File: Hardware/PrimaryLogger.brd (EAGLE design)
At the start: 52.1 x 77.1 mm, 72 parts, among them J1 CONN_42.54_SCREW, J2 CONN_42.54_SCREW, J3 CONN_42.54_SCREW, J4 CONN_42.54_SCREW, J5 CONN_32.54_SCREW, Q1 DMG3404, Q2 DMG3404, U1 MIC2005, U2 MIC2005, U25 SN74AUP3G34DCU, U3 TPL5010DDC, U4 TXS0102DCU, U5 SN74LVC1G3157SC70, U6 TCS3400, U7 SHTC3DFN, U8 MCP23008QFN, U9 MCP7940SOIC

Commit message: Documentation and folder structure updates
Moved around the folder structure, added board pictures, and added to README
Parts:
- JP1, JP2, JP3, JP4, JP5, JP6, JP8: device bschulz:SMT-JUMPER_3_1-NC_PASTE_SILK -> SparkFun-Jumpers:SMT-JUMPER_3_1-NC_PASTE_SILK
- JP10: device bschulz:SMT-JUMPER_2_NO_SILK -> SparkFun-Jumpers:SMT-JUMPER_2_NO_SILK
- JP7, JP9: device bschulz:SMT-JUMPER_2_NC_PASTE_SILK -> SparkFun-Jumpers:SMT-JUMPER_2_NC_PASTE_SILK
- R8: value 10k -> 100k

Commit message: Further documentation updates
Moved production files around, updated BoM in hardware and part libraries links to support that (DNP values issue)
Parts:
- JP1, JP2, JP3, JP4, JP5, JP6, JP8: device SparkFun-Jumpers:SMT-JUMPER_3_1-NC_PASTE_SILK -> bschulz:SMT-JUMPER_3_1-NC_PASTE_SILK
- JP10: device SparkFun-Jumpers:SMT-JUMPER_2_NO_SILK -> bschulz:SMT-JUMPER_2_NO_SILK
- JP9: device SparkFun-Jumpers:SMT-JUMPER_2_NC_PASTE_SILK -> bschulz:SMT-JUMPER_2_NC_PASTE_SILK
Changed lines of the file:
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@@
 <layer number="115" name="ReferenceISLANDS" color="7" fill="1" visible="no" active="yes"/>
 <layer number="116" name="Patch_BOT" color="7" fill="1" visible="no" active="yes"/>
+<layer number="117" name="PM_Ref" color="7" fill="1" visible="no" active="no"/>
 <layer number="118" name="Rect_Pads" color="7" fill="1" visible="no" active="yes"/>
+<layer number="119" name="PF_Ref" color="7" fill="1" visible="no" active="no"/>
+<layer number="120" name="WFL_Ref" color="7" fill="1" visible="no" active="no"/>
 <layer number="121" name="_tsilk" color="7" fill="1" visible="no" active="yes"/>
 <layer number="122" name="_bsilk" color="7" fill="1" visible="no" active="yes"/>
@@
 <attribute name="NAME" x="11.557" y="22.098" size="0.6096" layer="25" font="vector" ratio="15" rot="R90" align="center"/>
 </element>
-<element name="JP1" library="SparkFun-Jumpers" library_urn="urn:adsk.eagle:library:528" package="SMT-JUMPER_3_1-NC_PASTE_SILK" package3d_urn="urn:adsk.eagle:package:39293/1" value="JUMPER-SMT_3_1-NC_PASTE_SILK" x="30.48" y="51.181" smashed="yes" rot="MR90">
+<element name="JP1" library="bschulz" package="SMT-JUMPER_3_1-NC_PASTE_SILK" package3d_urn="urn:adsk.eagle:package:39293/1" value="JUMPER-SMT_3_1-NC_PASTE_SILK" x="30.48" y="51.181" smashed="yes" rot="MR90">
+<attribute name="DIGIKEY" value="DNP" x="30.48" y="51.181" size="1.778" layer="28" rot="MR90" display="off"/>
+<attribute name="MF" value="N/A" x="30.48" y="51.181" size="1.778" layer="28" rot="MR90" display="off"/>
+<attribute name="MPN" value="N/A" x="30.48" y="51.181" size="1.778" layer="28" rot="MR90" display="off"/>
 <attribute name="NAME" x="31.623" y="51.181" size="0.6096" layer="26" font="vector" ratio="20" rot="MR90" align="bottom-center"/>
 </element>
-<element name="JP2" library="SparkFun-Jumpers" library_urn="urn:adsk.eagle:library:528" package="SMT-JUMPER_3_1-NC_PASTE_SILK" package3d_urn="urn:adsk.eagle:package:39293/1" value="JUMPER-SMT_3_1-NC_PASTE_SILK" x="30.48" y="47.879" smashed="yes" rot="MR90">
+<element name="JP2" library="bschulz" package="SMT-JUMPER_3_1-NC_PASTE_SILK" package3d_urn="urn:adsk.eagle:package:39293/1" value="JUMPER-SMT_3_1-NC_PASTE_SILK" x="30.48" y="47.879" smashed="yes" rot="MR90">
+<attribute name="DIGIKEY" value="DNP" x="30.48" y="47.879" size="1.778" layer="28" rot="MR90" display="off"/>
+<attribute name="MF" value="N/A" x="30.48" y="47.879" size="1.778" layer="28" rot="MR90" display="off"/>
+<attribute name="MPN" value="N/A" x="30.48" y="47.879" size="1.778" layer="28" rot="MR90" display="off"/>
 <attribute name="NAME" x="31.623" y="47.879" size="0.6096" layer="26" font="vector" ratio="20" rot="MR90" align="bottom-center"/>
 </element>
-<element name="JP3" library="SparkFun-Jumpers" library_urn="urn:adsk.eagle:library:528" package="SMT-JUMPER_3_1-NC_PASTE_SILK" package3d_urn="urn:adsk.eagle:package:39293/1" value="JUMPER-SMT_3_1-NC_PASTE_SILK" x="30.48" y="39.751" smashed="yes" rot="MR90">
+<element name="JP3" library="bschulz" package="SMT-JUMPER_3_1-NC_PASTE_SILK" package3d_urn="urn:adsk.eagle:package:39293/1" value="JUMPER-SMT_3_1-NC_PASTE_SILK" x="30.48" y="39.751" smashed="yes" rot="MR90">
+<attribute name="DIGIKEY" value="DNP" x="30.48" y="39.751" size="1.778" layer="28" rot="MR90" display="off"/>
+<attribute name="MF" value="N/A" x="30.48" y="39.751" size="1.778" layer="28" rot="MR90" display="off"/>
+<attribute name="MPN" value="N/A" x="30.48" y="39.751" size="1.778" layer="28" rot="MR90" display="off"/>
 <attribute name="NAME" x="31.623" y="39.751" size="0.6096" layer="26" font="vector" ratio="20" rot="MR90" align="bottom-center"/>
 </element>
-<element name="JP4" library="SparkFun-Jumpers" library_urn="urn:adsk.eagle:library:528" package="SMT-JUMPER_3_1-NC_PASTE_SILK" package3d_urn="urn:adsk.eagle:package:39293/1" value="JUMPER-SMT_3_1-NC_PASTE_SILK" x="30.48" y="36.449" smashed="yes" rot="MR90">
+<element name="JP4" library="bschulz" package="SMT-JUMPER_3_1-NC_PASTE_SILK" package3d_urn="urn:adsk.eagle:package:39293/1" value="JUMPER-SMT_3_1-NC_PASTE_SILK" x="30.48" y="36.449" smashed="yes" rot="MR90">
+<attribute name="DIGIKEY" value="DNP" x="30.48" y="36.449" size="1.778" layer="28" rot="MR90" display="off"/>
+<attribute name="MF" value="N/A" x="30.48" y="36.449" size="1.778" layer="28" rot="MR90" display="off"/>
+<attribute name="MPN" value="N/A" x="30.48" y="36.449" size="1.778" layer="28" rot="MR90" display="off"/>
 <attribute name="NAME" x="31.623" y="36.449" size="0.6096" layer="26" font="vector" ratio="20" rot="MR90" align="bottom-center"/>
 </element>
-<element name="JP5" library="SparkFun-Jumpers" library_urn="urn:adsk.eagle:library:528" package="SMT-JUMPER_3_1-NC_PASTE_SILK" package3d_urn="urn:adsk.eagle:package:39293/1" value="JUMPER-SMT_3_1-NC_PASTE_SILK" x="30.48" y="28.321" smashed="yes" rot="MR90">
+<element name="JP5" library="bschulz" package="SMT-JUMPER_3_1-NC_PASTE_SILK" package3d_urn="urn:adsk.eagle:package:39293/1" value="JUMPER-SMT_3_1-NC_PASTE_SILK" x="30.48" y="28.321" smashed="yes" rot="MR90">
+<attribute name="DIGIKEY" value="DNP" x="30.48" y="28.321" size="1.778" layer="28" rot="MR90" display="off"/>
+<attribute name="MF" value="N/A" x="30.48" y="28.321" size="1.778" layer="28" rot="MR90" display="off"/>
+<attribute name="MPN" value="N/A" x="30.48" y="28.321" size="1.778" layer="28" rot="MR90" display="off"/>
 <attribute name="NAME" x="31.623" y="28.321" size="0.6096" layer="26" font="vector" ratio="20" rot="MR90" align="bottom-center"/>
 </element>
-<element name="JP6" library="SparkFun-Jumpers" library_urn="urn:adsk.eagle:library:528" package="SMT-JUMPER_3_1-NC_PASTE_SILK" package3d_urn="urn:adsk.eagle:package:39293/1" value="JUMPER-SMT_3_1-NC_PASTE_SILK" x="30.48" y="25.019" smashed="yes" rot="MR90">
+<element name="JP6" library="bschulz" package="SMT-JUMPER_3_1-NC_PASTE_SILK" package3d_urn="urn:adsk.eagle:package:39293/1" value="JUMPER-SMT_3_1-NC_PASTE_SILK" x="30.48" y="25.019" smashed="yes" rot="MR90">
+<attribute name="DIGIKEY" value="DNP" x="30.48" y="25.019" size="1.778" layer="28" rot="MR90" display="off"/>
+<attribute name="MF" value="N/A" x="30.48" y="25.019" size="1.778" layer="28" rot="MR90" display="off"/>
+<attribute name="MPN" value="N/A" x="30.48" y="25.019" size="1.778" layer="28" rot="MR90" display="off"/>
 <attribute name="NAME" x="31.623" y="25.019" size="0.6096" layer="26" font="vector" ratio="20" rot="MR90" align="bottom-center"/>
 </element>
@@
 <attribute name="VALUE_PART" value="100k" x="13.716" y="31.496" size="1.778" layer="27" rot="R180" display="off"/>
 </element>
-<element name="JP8" library="SparkFun-Jumpers" library_urn="urn:adsk.eagle:library:528" package="SMT-JUMPER_3_1-NC_PASTE_SILK" package3d_urn="urn:adsk.eagle:package:39293/1" value="JUMPER-SMT_3_1-NC_PASTE_SILK" x="30.48" y="44.577" smashed="yes" rot="MR270">
+<element name="JP8" library="bschulz" package="SMT-JUMPER_3_1-NC_PASTE_SILK" package3d_urn="urn:adsk.eagle:package:39293/1" value="JUMPER-SMT_3_1-NC_PASTE_SILK" x="30.48" y="44.577" smashed="yes" rot="MR270">
+<attribute name="DIGIKEY" value="DNP" x="30.48" y="44.577" size="1.778" layer="28" rot="MR270" display="off"/>
+<attribute name="MF" value="N/A" x="30.48" y="44.577" size="1.778" layer="28" rot="MR270" display="off"/>
+<attribute name="MPN" value="N/A" x="30.48" y="44.577" size="1.778" layer="28" rot="MR270" display="off"/>
 <attribute name="NAME" x="31.623" y="44.577" size="0.6096" layer="26" font="vector" ratio="20" rot="MR90" align="bottom-center"/>
 </element>
@@
 <attribute name="VALUE_PART" value="100k" x="25.908" y="51.816" size="1.778" layer="27" display="off"/>
 </element>
-<element name="JP9" library="SparkFun-Jumpers" library_urn="urn:adsk.eagle:library:528" package="SMT-JUMPER_2_NC_PASTE_SILK" package3d_urn="urn:adsk.eagle:package:39282/1" value="JUMPER-SMT_2_NC_PASTE_SILK" x="27.051" y="52.197" smashed="yes" rot="MR180">
+<element name="JP9" library="bschulz" package="SMT-JUMPER_2_NC_PASTE_SILK" package3d_urn="urn:adsk.eagle:package:39282/1" value="JUMPER-SMT_2_NC_PASTE_SILK" x="27.051" y="52.197" smashed="yes" rot="MR180">
+<attribute name="DIGIKEY" value="DNP" x="27.051" y="52.197" size="1.778" layer="28" rot="MR180" display="off"/>
+<attribute name="MF" value="N/A" x="27.051" y="52.197" size="1.778" layer="28" rot="MR180" display="off"/>
+<attribute name="MPN" value="N/A" x="27.051" y="52.197" size="1.778" layer="28" rot="MR180" display="off"/>
 <attribute name="NAME" x="27.051" y="51.054" size="0.6096" layer="26" font="vector" ratio="20" rot="MR180" align="bottom-center"/>
 <attribute name="VALUE" x="27.051" y="53.34" size="0.6096" layer="28" font="vector" ratio="20" rot="MR180" align="top-center"/>
 </element>
-<element name="JP10" library="SparkFun-Jumpers" library_urn="urn:adsk.eagle:library:528" package="SMT-JUMPER_2_NO_SILK" package3d_urn="urn:adsk.eagle:package:39279/1" value="JUMPER-SMT_2_NO_SILK" x="2.667" y="59.309" smashed="yes" rot="R270">
+<element name="JP10" library="bschulz" package="SMT-JUMPER_2_NO_SILK" package3d_urn="urn:adsk.eagle:package:39279/1" value="JUMPER-SMT_2_NO_SILK" x="2.667" y="59.309" smashed="yes" rot="R270">
+<attribute name="DIGIKEY" value="DNP" x="2.667" y="59.309" size="1.778" layer="27" rot="R270" display="off"/>
+<attribute name="MF" value="N/A" x="2.667" y="59.309" size="1.778" layer="27" rot="R270" display="off"/>
+<attribute name="MPN" value="N/A" x="2.667" y="59.309" size="1.778" layer="27" rot="R270" display="off"/>
 <attribute name="NAME" x="2.667" y="58.039" size="0.6096" layer="25" font="vector" ratio="20" rot="R180" align="bottom-center"/>
 </element>

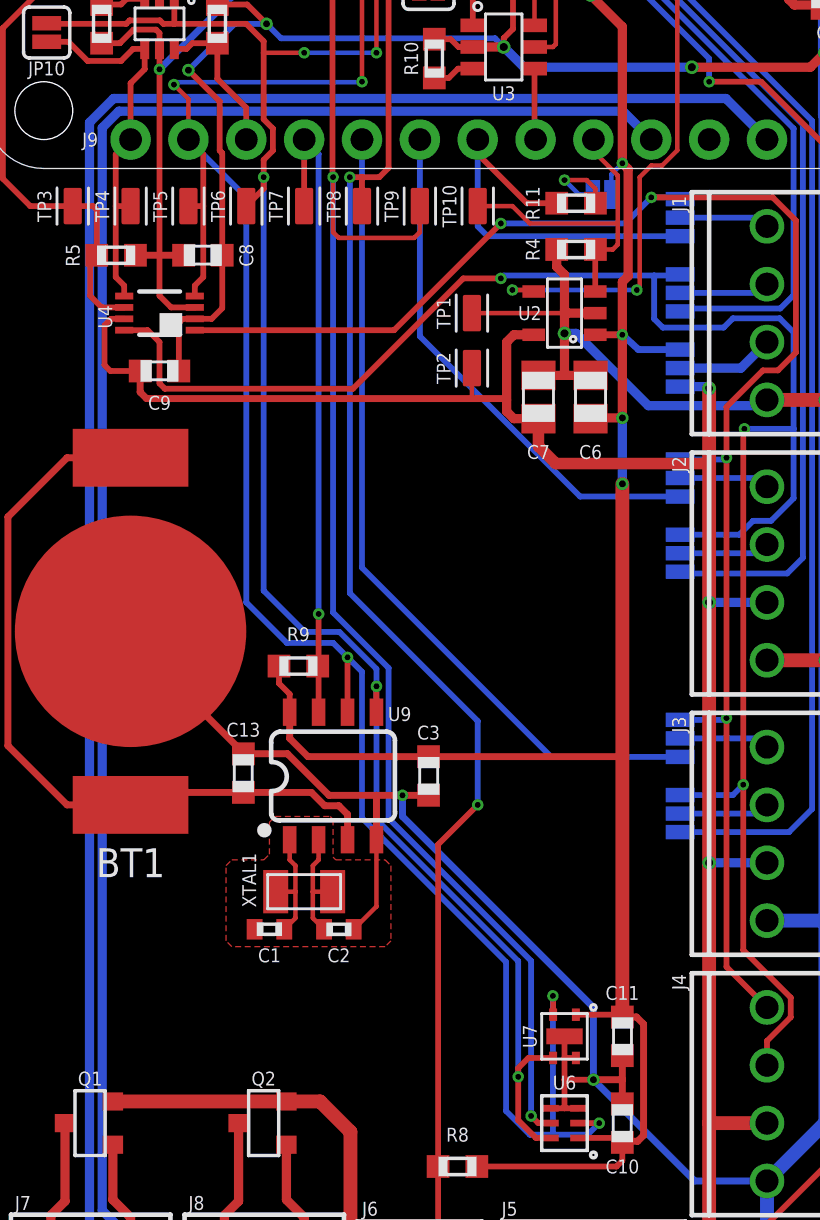
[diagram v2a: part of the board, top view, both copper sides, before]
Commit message: Added LED support for v0.3
Schematic capture and preliminary layout of LED indicator
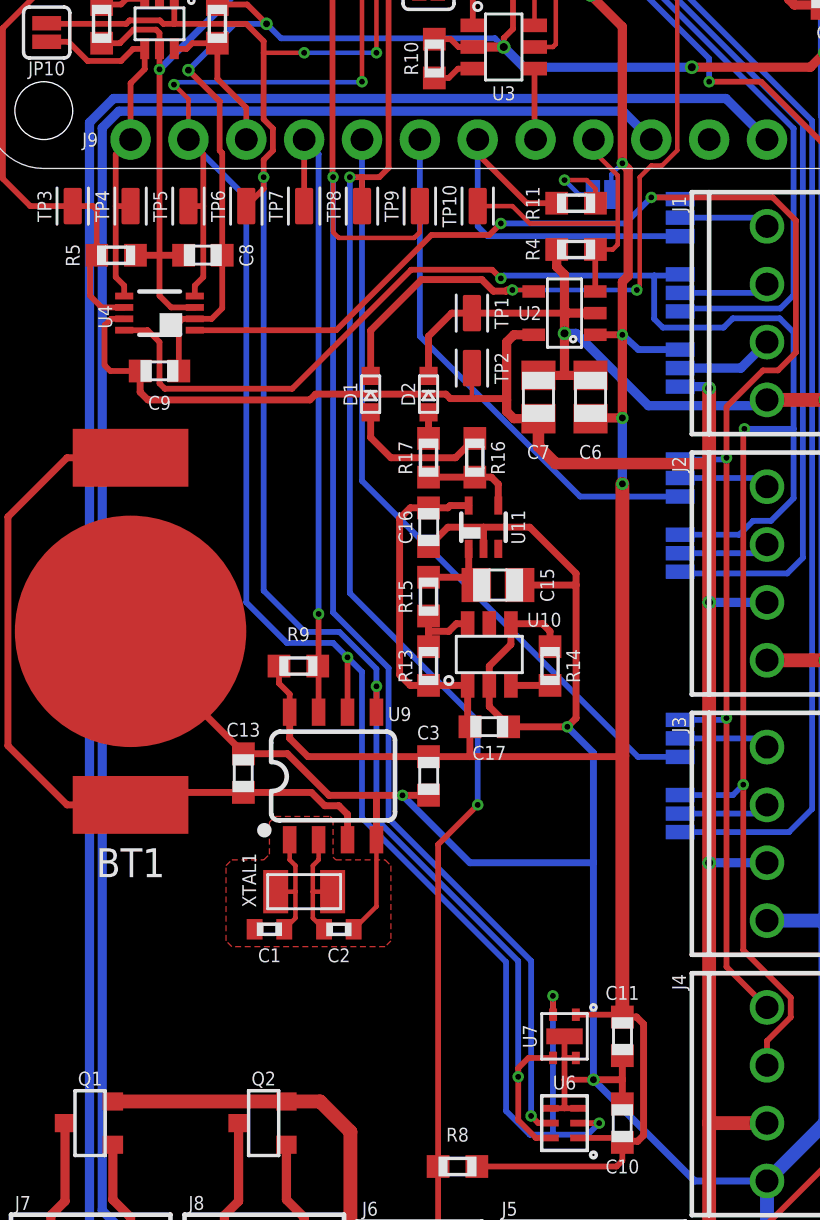
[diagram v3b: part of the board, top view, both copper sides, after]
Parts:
- added C15: 10uF, bschulz_passives:C0805
- added C16, C17: 0.1uF, bschulz_passives:C0603
- added D1, D2: LED0603, bschulz:LED_0603
- added R13, R14, R15: 10k, bschulz_passives:R0603
- added R16, R17: 4.7k, bschulz_passives:R0603
- added U10: TPL5010DDC, bschulz:DDC_R-PDSO-G6
- added U11: MIC842, bschulz:DCK_R-PDSO-G5
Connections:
- new net N$10: R16.2, R17.2, U11.4
- new net N$11: D1.ANODE, R16.1
- new net N$12: D2.ANODE, R17.1
- new net N$7: R14.2, U10.3
- new net N$8: C15.1, R15.2, U11.1
- new net N$9: R13.1, R15.1, U10.6
- net 3V3: now also C16.1, C17.1, R13.2, U10.1, U11.5
- net 3V3_EXT_FAULT: now also D1.CATHODE
- net GND: now also C15.2, C16.2, C17.2, D2.CATHODE, R14.1, U10.2, U10.4, U11.2
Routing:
- net GND: track 332.8 -> 375.4 mm, vias 12 -> 13
- net 3V3: track 184.9 -> 201.4 mm
- net 3V3_EXT_FAULT: track 32.6 -> 42.0 mm
- net N$11: track 0.00 -> 6.40 mm
- net N$10: track 0.00 -> 4.13 mm
- net N$8: track 0.00 -> 3.97 mm
- net N$9: track 0.00 -> 3.20 mm
- net GPIO3D: track 36.2 -> 34.0 mm
- net N$7: track 0.00 -> 1.72 mm
- net N$12: track 0.00 -> 1.14 mm
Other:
- board text added: "FAULT"
- board text added: "PWR"

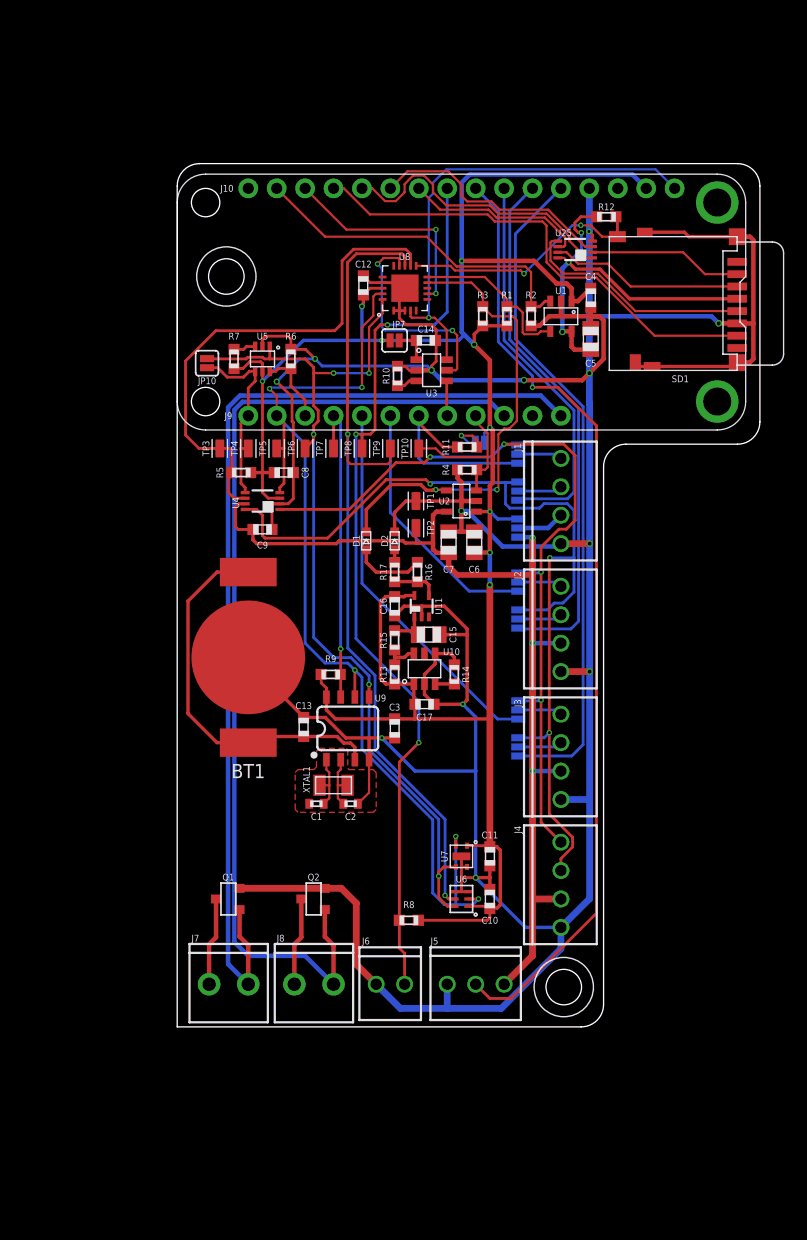
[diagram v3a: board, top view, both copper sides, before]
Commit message: Updated IO expander to SSOP package
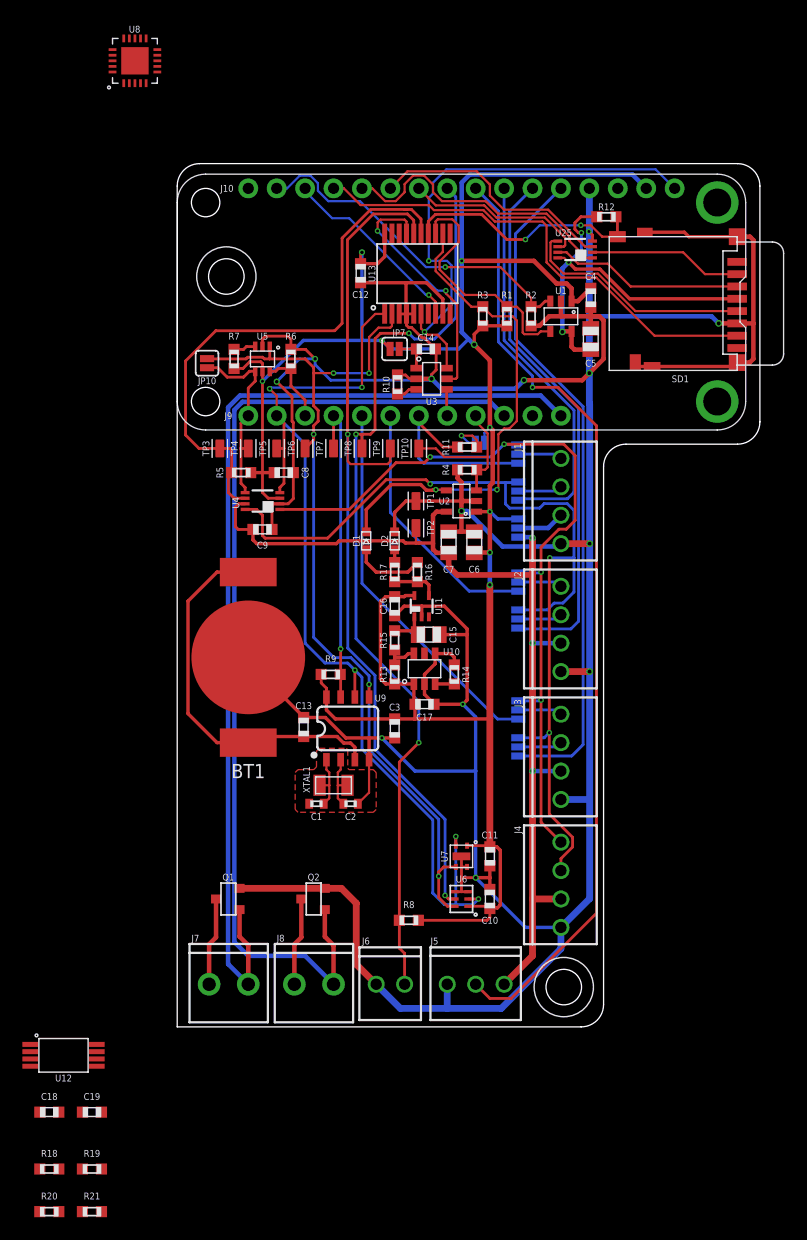
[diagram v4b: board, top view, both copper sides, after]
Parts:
- added C18, C19: 0.1uF, bschulz_passives:C0603
- added R18, R19, R20, R21: (no value), bschulz_passives:R0603
- added U12: PCA9617TSSOP8, bschulz:TTSOP_8
- added U13: MCP23008SSOP, bschulz:SSOP20
- moved U8 31.5 mm to (-3.81, 86.4)
- moved C12 1.12 mm to (16.4, 67.3), turned to 270 degrees
- moved C14 0.76 mm to (22.2, 60.6)
- moved JP7 0.76 mm to (19.4, 60.6)
- moved U3 0.76 mm to (22.7, 57.9)
- moved R10 0.76 mm to (19.7, 57.4)
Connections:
- new net SCL_IN: R18.1
- new net SCL_OUT: R20.1
- new net SDA_IN: R19.1
- new net SDA_OUT: R21.1
- new net VCC_IN: C18.1, R18.2, R19.2
- new net VCC_OUT: C19.1, R20.2, R21.2
- net 3V3: now also U12.8, U13.20
- net 3V3_EXT: now also U12.1
- net 3V3_EXT_FAULT: now also U13.12
- net 3V3_SD_FAULT: now also U13.13
- net GND: now also C18.2, C19.2, U12.4, U13.3, U13.4, U13.5, U13.9
- net I2C_EXT_EN: now also U12.5, U13.15
- net IO_EXP_INT: now also U13.8
- net PAR_INT: now also U13.16
- net RST: now also U13.6
- net SCL: now also U12.7, U13.1
- net SCL_EXT: now also U12.2
- net SDA: now also U12.6
- net SDA_EXT: now also U12.3
- net SDA_OB: now also U13.2
- net SD_CD: now also U13.14
- net WAKE: now also U13.17
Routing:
- net 3V3: track 201.4 -> 210.0 mm
- net 3V3_SD_FAULT: track 14.7 -> 21.5 mm
- net GND: track 375.4 -> 381.7 mm
- net I2C_EXT_EN: track 45.8 -> 49.8 mm
- net PAR_INT: track 75.1 -> 79.0 mm
- net RST: track 41.9 -> 45.4 mm, vias 1 -> 2
- net 3V3_EXT_FAULT: track 42.0 -> 44.7 mm
- net IO_EXP_INT: track 19.7 -> 17.1 mm, vias 2 -> 1
- net WAKE: track 19.6 -> 22.0 mm
- net SCL: track 93.0 -> 91.4 mm
- net TIP: track 82.6 -> 83.9 mm
- net WD_HOLD: track 3.13 -> 2.37 mm
- net 3V3_SD_EN: track 30.8 -> 30.9 mm, vias 0 -> 1
